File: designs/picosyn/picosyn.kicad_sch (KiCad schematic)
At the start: 20 parts, among them J1 Midi DIN, J2 AudioJack2, U1 H11L1, U2 74HC4051

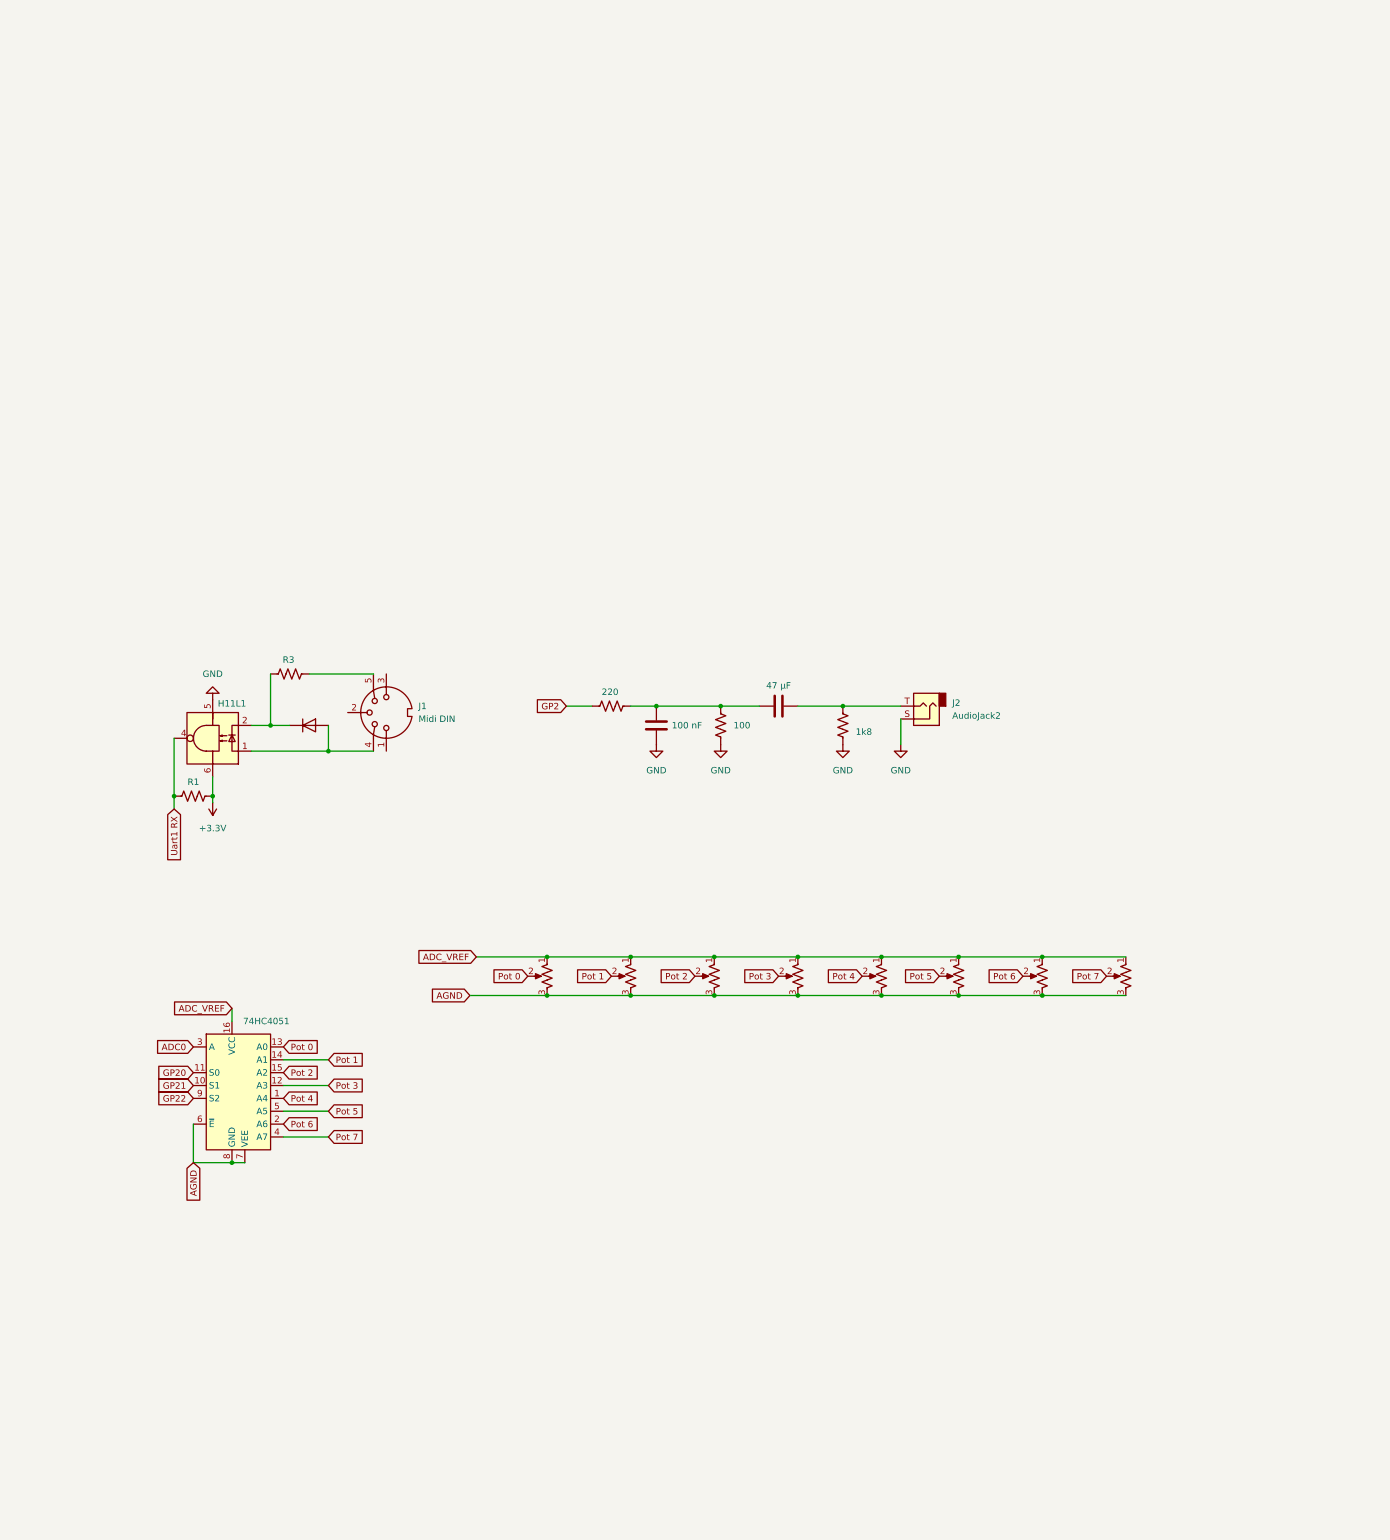
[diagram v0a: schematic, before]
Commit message: cleaned up code
i also spilt it into more files for easier access. i think that's all.
for hardware, it's a mess. i changed breadboards, but it turns out that
the new one doesn't conduct electricity where it needs to. i will need
to change it back. that is the main reason for it not working. i think.
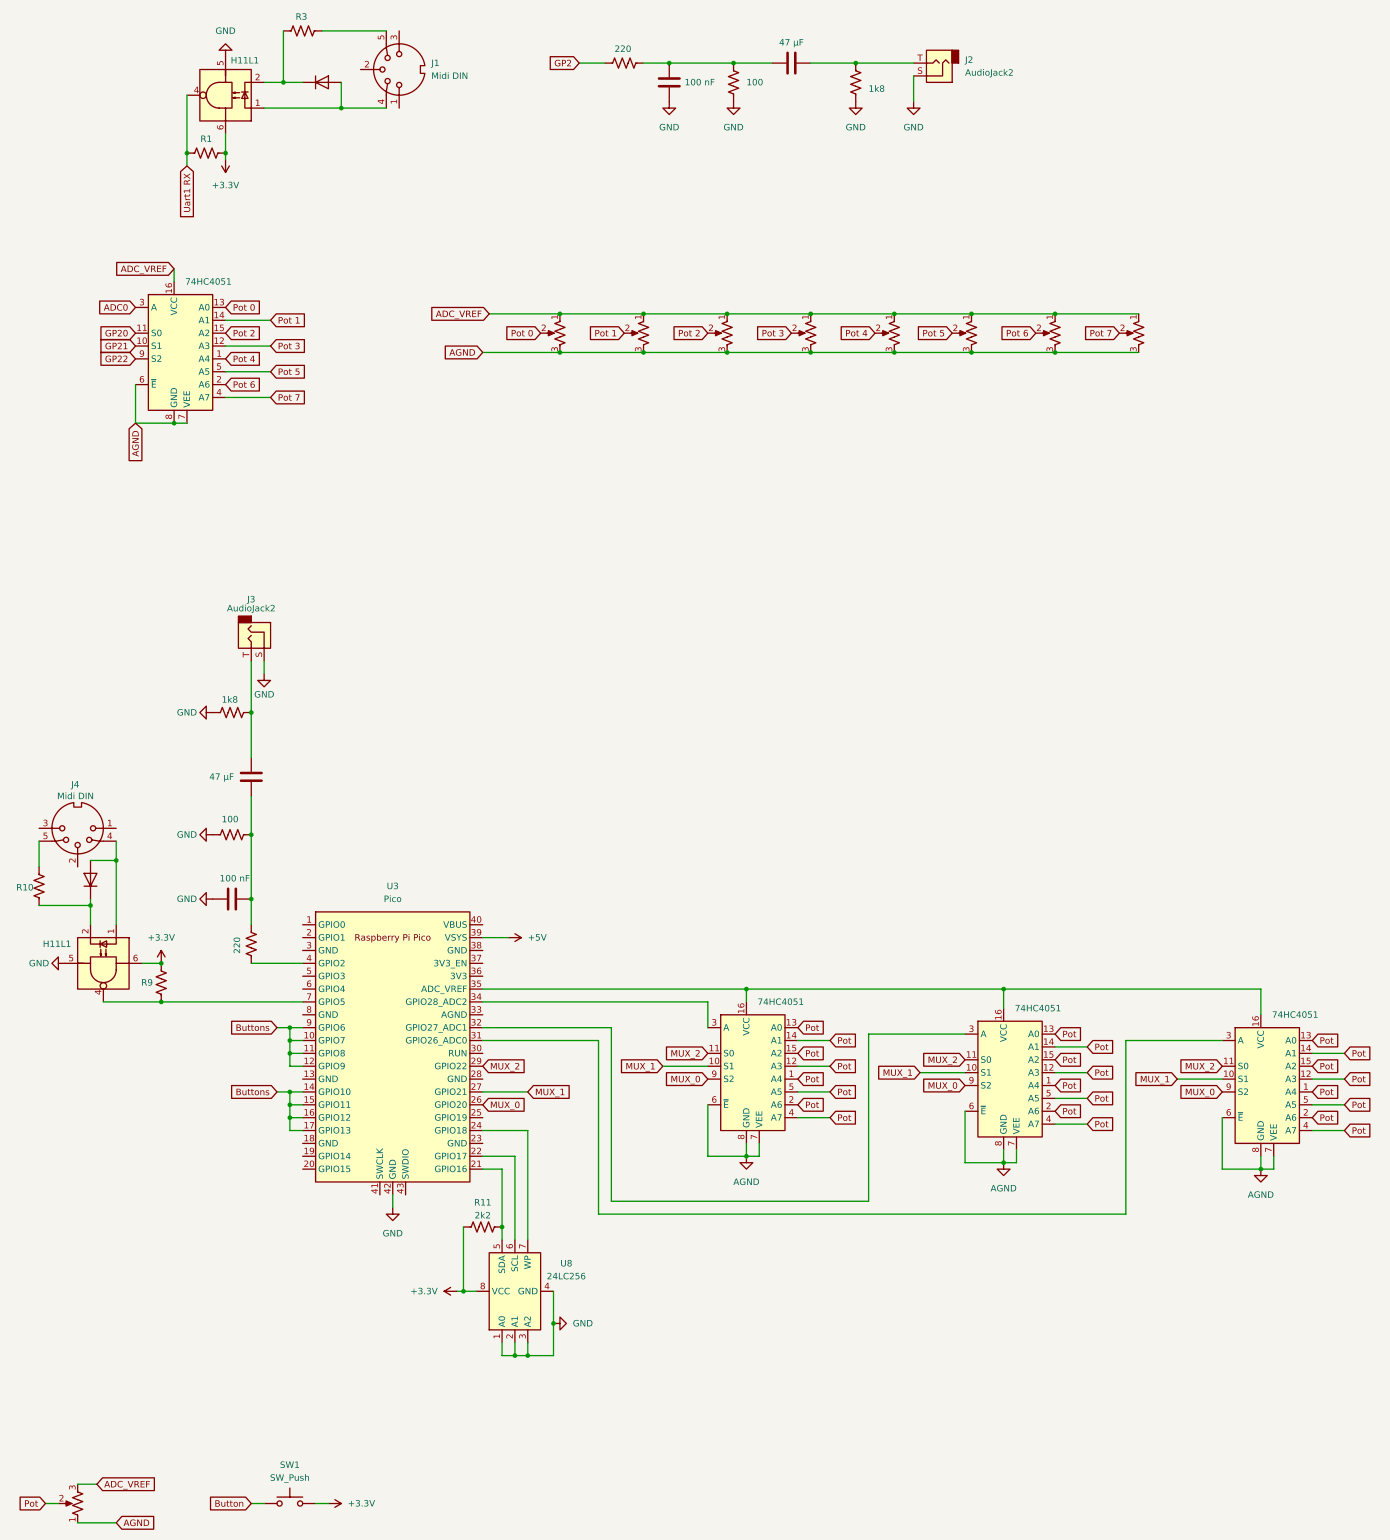
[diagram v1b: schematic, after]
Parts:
- added C3: 100 nF, symbol Device:C
- added C4: 47 µF, symbol Device:C
- added D2: 1N4148, Diode_THT:D_DO-35_SOD27_P7.62mm_Horizontal, symbol Diode:1N4148
- added J3: AudioJack2, symbol Connector_Audio:AudioJack2
- added J4: Midi DIN, symbol Connector:DIN-5_180degree
- added R10, R9: R_US, symbol Device:R_US
- added R11: 2k2, symbol Device:R_US
- added R6: 220, symbol Device:R_US
- added R7: 100, symbol Device:R_US
- added R8: 1k8, symbol Device:R_US
- added RV17: R_Potentiometer_US, symbol Device:R_Potentiometer_US
- added SW1: SW_Push, symbol Switch:SW_Push
- added U3: Pico, RPi_Pico:RPi_Pico_SMD_TH, symbol MCU_RaspberryPi_and_Boards:Pico
- added U4, U5, U6: 74HC4051, symbol 74xx:74HC4051
- added U7: H11L1, symbol Isolator:H11L1
- added U8: 24LC256, symbol Memory_EEPROM:24LC256
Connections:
- net +3.3V: now also R11.2, R9.2, SW1.1, U7.6, U8.8 (VCC)
- net ADC_VREF: now also RV17.3
- net AGND: now also RV17.1, U4.6 (~{E}), U4.7 (VEE), U4.8 (GND), U5.6 (~{E}), U5.7 (VEE), U5.8 (GND), U6.6 (~{E}), U6.7 (VEE), U6.8 (GND)
- net GND: now also C3.1, J3.S, R7.1, R8.1, U3.42 (GND), U7.5, U8.1 (A0), U8.2 (A1), U8.3 (A2), U8.4 (GND)
- new net: U3.35 (ADC_VREF), U4.16 (VCC), U5.16 (VCC), U6.16 (VCC)
- new net: U3.34 (GPIO28_ADC2), U4.3 (A)
- new net: U3.32 (GPIO27_ADC1), U5.3 (A)
- new net: D2.1 (K), R10.1, U7.2
- new net: J4.5, R10.2
- new net: C3.2, C4.1, R6.2, R7.2
- new net: C4.2, J3.T, R8.2
- new net: U3.31 (GPIO26_ADC0), U6.3 (A)
- new net: R6.1, U3.4 (GPIO2)
- new net: D2.2 (A), J4.4, U7.1
- new net: R11.1, U3.21 (GPIO16), U8.5 (SDA)
- new net: U3.22 (GPIO17), U8.6 (SCL)
- new net: U3.24 (GPIO18), U8.7 (WP)
- new net: R9.1, U3.7 (GPIO5), U7.4
- new net +5V: U3.39 (VSYS)
- new net Button: SW1.2
- new net Buttons: U3.10 (GPIO7), U3.11 (GPIO8), U3.12 (GPIO9), U3.14 (GPIO10), U3.15 (GPIO11), U3.16 (GPIO12), U3.17 (GPIO13), U3.9 (GPIO6)
- new net MUX_0: U3.26 (GPIO20), U4.9 (S2), U5.9 (S2), U6.9 (S2)
- new net MUX_1: U3.27 (GPIO21), U4.10 (S1), U5.10 (S1), U6.10 (S1)
- new net MUX_2: U3.29 (GPIO22), U4.11 (S0), U5.11 (S0), U6.11 (S0)
- new net Pot: RV17.2, U4.1 (A4), U4.12 (A3), U4.13 (A0), U4.14 (A1), U4.15 (A2), U4.2 (A6), U4.4 (A7), U4.5 (A5), U5.1 (A4), U5.12 (A3), U5.13 (A0), U5.14 (A1), U5.15 (A2), U5.2 (A6), U5.4 (A7), U5.5 (A5), U6.1 (A4), U6.12 (A3), U6.13 (A0), U6.14 (A1), U6.15 (A2), U6.2 (A6), U6.4 (A7), U6.5 (A5)
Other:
- moved on the sheet: J1, J2, R1, R3
